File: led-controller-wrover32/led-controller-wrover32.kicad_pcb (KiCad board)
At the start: 4 copper layers, 36 x 43 mm, 82 parts, among them J1 Micro_SD_Card, J10 Conn_01x02 DNF, J101 Conn_01x02, J11 Conn_01x02, J2 BM12B-SRSS-TBT(LF)(SN), J3 USB_B_Micro, J4 BM12B-SRSS-TBT(LF)(SN), J5 Conn_01x04, J6 Conn_01x02 DNF, J7 Conn_01x02 DNF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

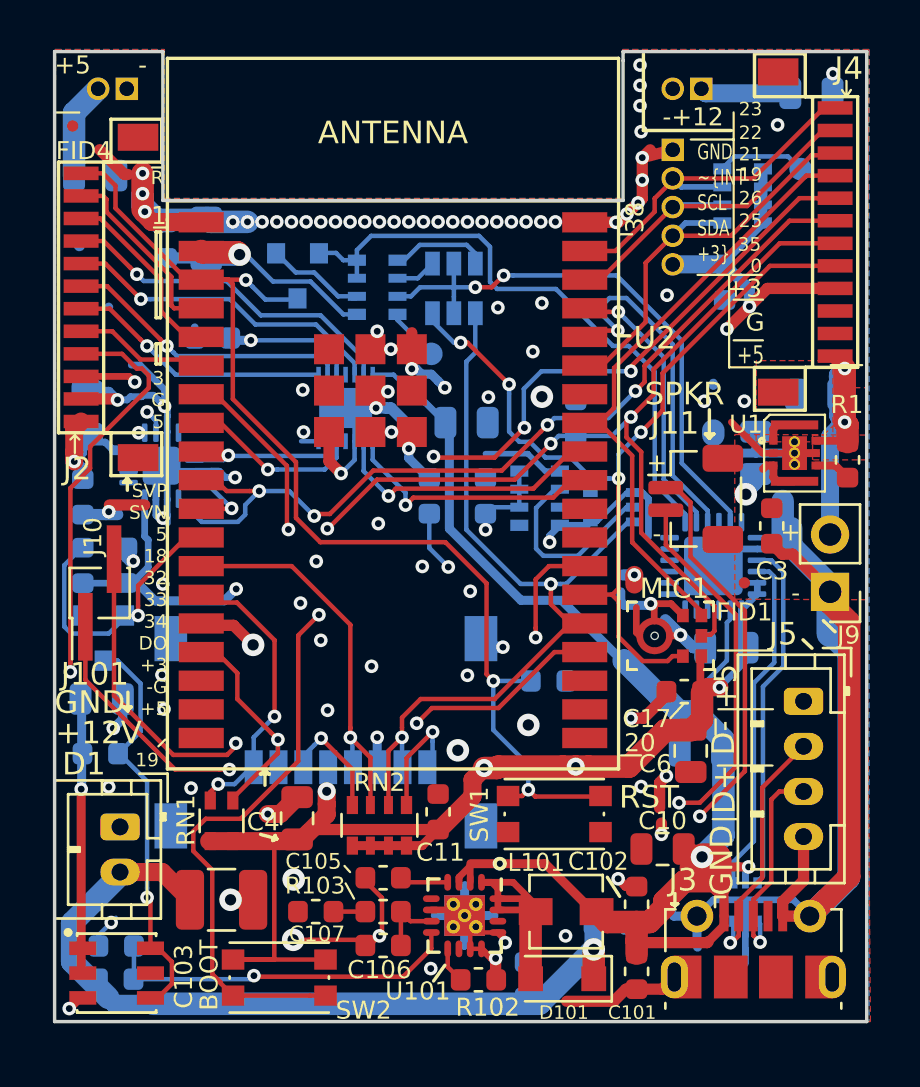
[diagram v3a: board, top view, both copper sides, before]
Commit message: Multiple changes from v3.7
1. Fixed microphone so it uses the left channel
2. Reduced the number of unique components, i.e. replacing a couple of
   resistor networks with already used resistors
3. Removed unneeded resistor in programming circuit
4. Moved speaker chip to the other side to be closer to the connector
5. Cleaned up some of the traces and removed some inner-layer traces.
6. Moved reset switch to the edge to make access easier.
7. Added big via to line up with daughter card.
8. Replaced BSS138 transistor array with two BSS138 transistors to reduce
   the unique component count and reduce cost.

Signed-off-by: Aaron Williams <aaron.w2@gmail.com>
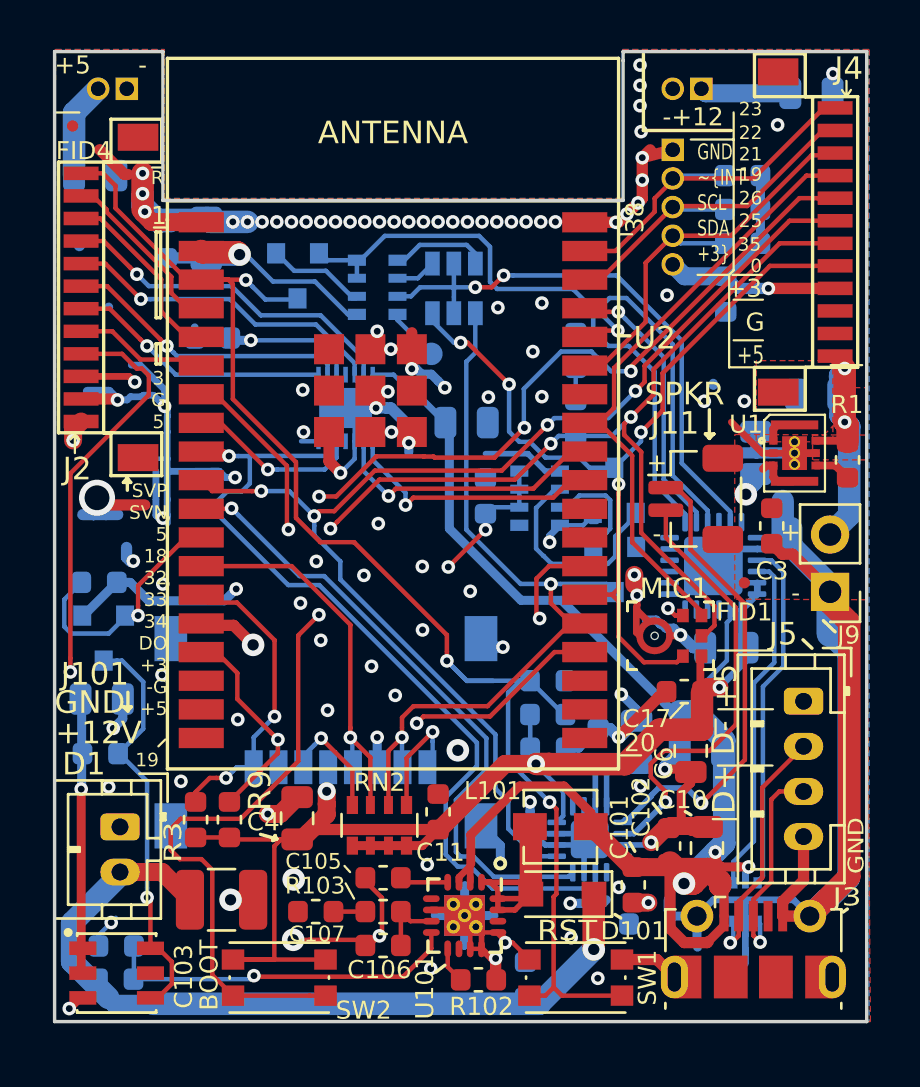
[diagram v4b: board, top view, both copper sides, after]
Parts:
- removed J10: Conn_01x02 DNF, Connector_PinHeader_1.27mm:PinHeader_1x02_P1.27mm_Vertical_SMD_Pin1Left
- removed RN1: 10K, Resistor_SMD:R_Array_Convex_2x0603
- removed RN3: 4.7K, Resistor_SMD:R_Array_Convex_4x0603
- removed TP1: DNF, TestPoint:TestPoint_Pad_D1.0mm
- added Q4: BSS138, Package_TO_SOT_SMD:SOT-23, B.Cu at (74.8, 61.5)
- added R11: 10K, Resistor_SMD:R_0603_1608Metric, B.Cu at (73.1, 55.2)
- added R4: 4.7K, Resistor_SMD:R_0603_1608Metric, B.Cu at (80.5, 47.5)
- added R7: 4.7K, Resistor_SMD:R_0603_1608Metric, B.Cu at (80.5, 49.0)
- added R8: 4.7K, Resistor_SMD:R_0603_1608Metric, B.Cu at (80.5, 50.5)
- added R9: 10K, Resistor_SMD:R_0603_1608Metric, F.Cu at (57.8, 76.0)
- Q5: value BSS138DW-7-F -> BSS138; footprint Package_TO_SOT_SMD:SOT-363_SC-70-6 -> Package_TO_SOT_SMD:SOT-23
- R10: value 100K -> 86.6K
- R3: moved to F.Cu
- RN6: value 100K -> 10K
- U2: value ESP32-WROVER -> ESP32-WROVER-B
- moved C20 28.4 mm to (75.8, 72.6)
- moved C21 25.4 mm to (74.1, 72.8), turned to 90 degrees
- moved U5 25.2 mm to (73.7, 76.9), turned to 0 degrees
- moved C22 20.4 mm to (71.9, 72.9), turned to 0 degrees
- moved R3 17.7 mm to (56.2, 76.0), turned to 270 degrees
- moved SW1 7.31 mm to (73.1, 83.0), turned to 0 degrees
- moved C101 3.84 mm to (75.7, 78.9)
- moved L101 3.77 mm to (72.4, 76.4)
- moved D101 3.75 mm to (72.5, 79.3)
- moved C102 2.94 mm to (77.2, 77.2)
- moved Q5 2.76 mm to (74.8, 65.0), turned to 270 degrees
- moved R2 2.32 mm to (71.9, 71.4), turned to 0 degrees
- moved C10 1.97 mm to (78.9, 77.3), turned to 90 degrees
- moved R5 1.04 mm to (52.0, 65.5), turned to 0 degrees
- moved C15 0.53 mm to (79.8, 52.8)
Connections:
- MIC1 pad 2: GND -> +3V3
- Q5 pad 1: GND -> /Reset_Boot/PGM_IO2_DRV
- Q5 pad 2: /Reset_Boot/PGM_IO2_DRV -> GND
- Q5 pad 3: IO0 -> IO2
- R10 pad 1: GND -> Net-(R10-Pad1)
- R3 pad 1: /Reset_Boot/~PGM_SW_OUT -> /IO12
- R3 pad 2: GND -> +3V3
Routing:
- net GND: track 286.2 -> 222.7 mm, vias 100 -> 108
- net /Amp/SPKR-: track 67.1 -> 19.7 mm, vias 3 -> 1
- net /Amp/SPKR+: track 66.6 -> 20.9 mm, vias 3 -> 1
- net IO33: track 7.92 -> 38.9 mm
- net IO26: track 37.3 -> 62.6 mm
- net IO25: track 39.3 -> 54.6 mm
- net ~RESET: track 51.6 -> 64.4 mm
- net VBUS: track 102.8 -> 107.5 mm
- net Net-(RN3-Pad4): track 3.94 -> 0.00 mm
- net /Reset_Boot/PGM_IO2_DRV: track 1.35 -> 4.91 mm
- net +3V3: track 111.0 -> 113.3 mm, vias 11 -> 10
- net +12V: track 83.1 -> 85.4 mm
- net IO2: track 37.3 -> 35.5 mm
- net /IO27: track 12.7 -> 11.1 mm
- net Net-(R10-Pad1): track 0.00 -> 1.42 mm
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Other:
- board text added: "Copyright © 2020 Aaron Williams"
- board text added: "Rev 3.8"
- board text removed: "Copyright © 2019 Aaron Williams"
- board text removed: "Rev 3.7"
